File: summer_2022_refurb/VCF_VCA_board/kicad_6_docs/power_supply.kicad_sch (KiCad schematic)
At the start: 47 parts, among them J7 power_entry, U1 TL072, U10 SSI2164, U11 SSI2164, U2 TL072, U3 TL072, U4 TL072, U5 TL072, U501 LM4040DBZ-5, U502 LM4040DBZ-5, U6 TL072, U7 TL072, U8 TL072, U9 TL072

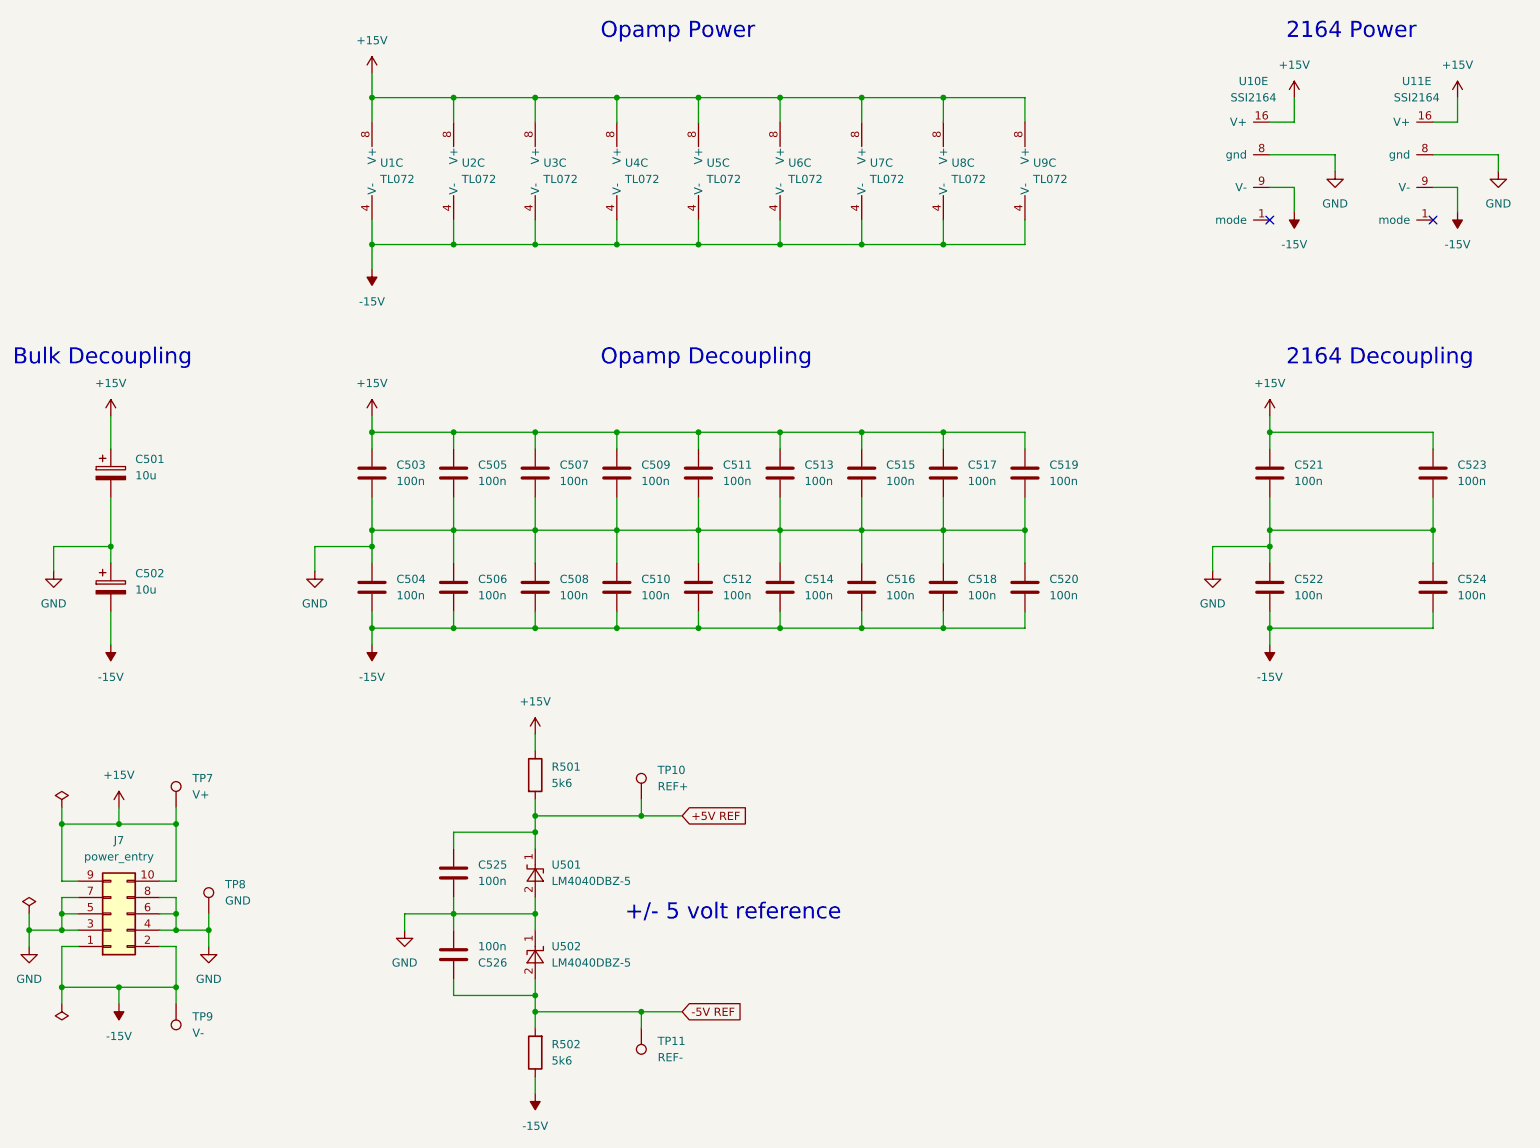
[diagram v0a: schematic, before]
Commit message: Change directory structure, minor schem and pcb tweaks
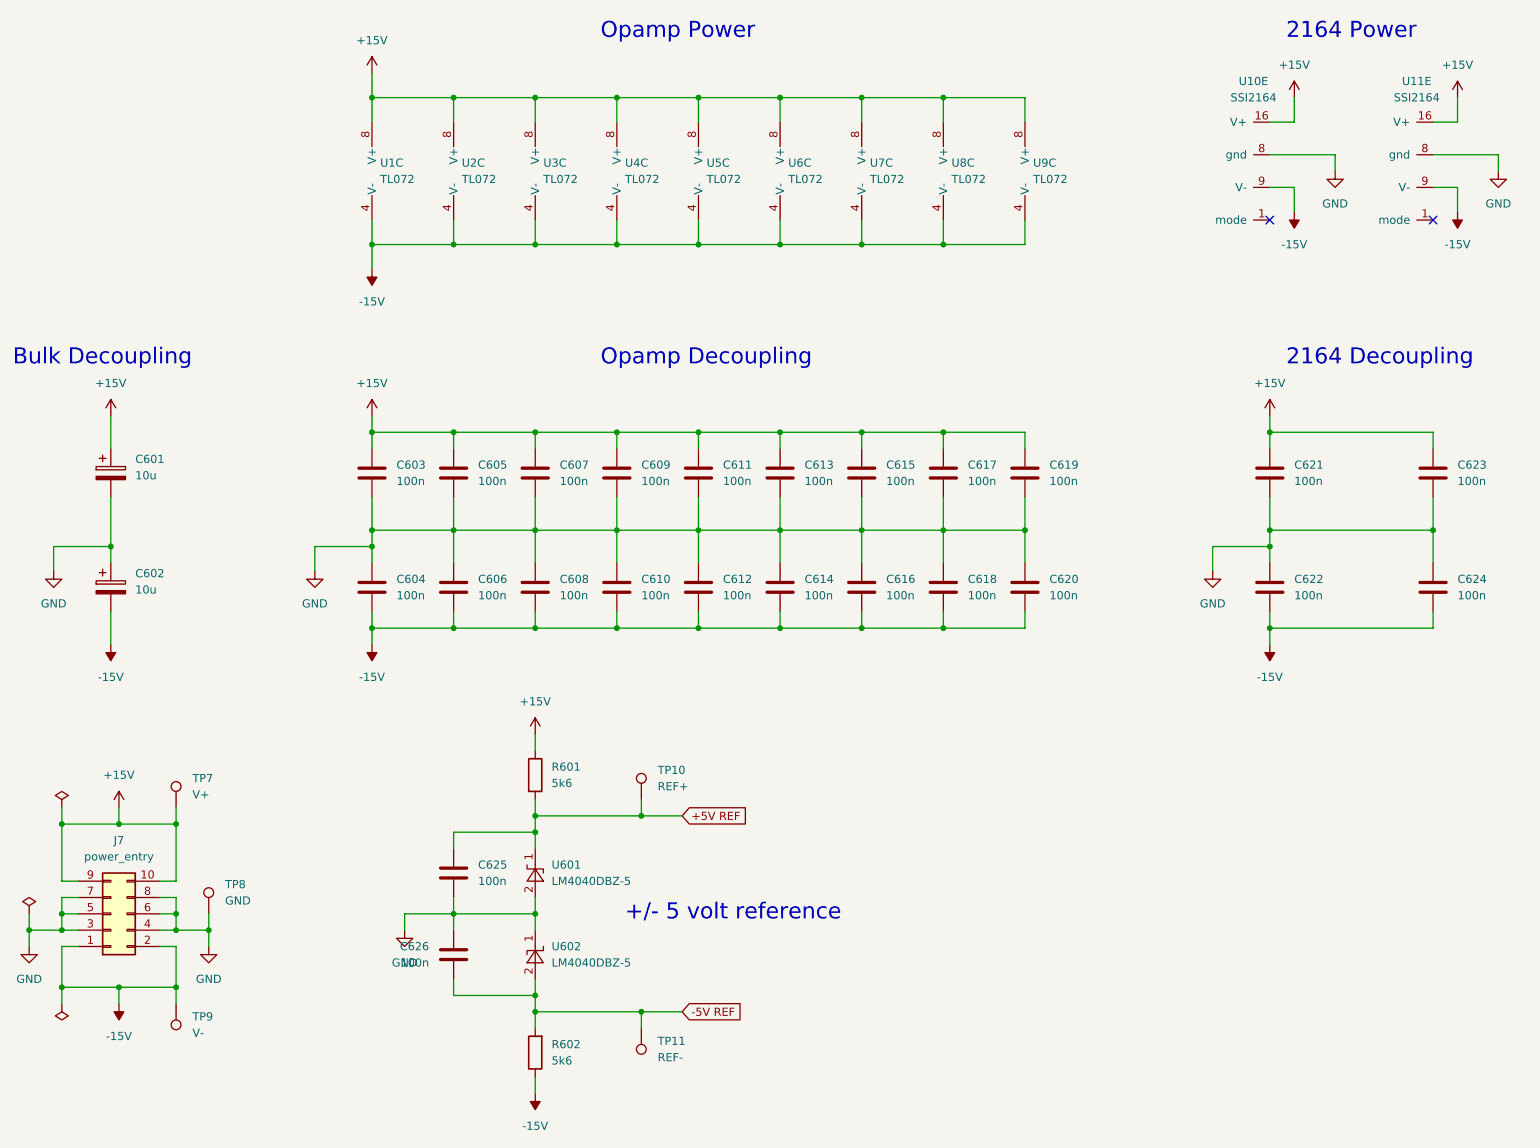
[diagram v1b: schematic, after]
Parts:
- TP10, TP11, TP7, TP8, TP9: now left out of the parts list
- renumbered C501 to C601, C502 to C602, C503 to C603, C504 to C604, C505 to C605, C506 to C606, C507 to C607, C508 to C608, C509 to C609, C510 to C610, C511 to C611, C512 to C612, C513 to C613, C514 to C614, C515 to C615, C516 to C616, C517 to C617, C518 to C618, C519 to C619, C520 to C620, C521 to C621, C522 to C622, C523 to C623, C524 to C624, C525 to C625, C526 to C626, R501 to R601, R502 to R602, U501 to U601, U502 to U602
